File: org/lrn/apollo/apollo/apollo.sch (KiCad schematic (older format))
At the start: 68 parts, among them J10 Conn_01x01_Male, J11 Conn_01x01_Male, J12 Conn_01x01_Male, J13 Conn_01x01_Male, J17 Conn_01x01_Male, J18 Conn_01x01_Male, J4 Conn_01x01_Male, J6 Conn_01x01_Male, J7 Conn_01x01_Male, J8 Conn_01x01_Male, J9 Conn_01x01_Male, Q1 PN2222A, Q2 PN2222A, Q3 PN2222A, Q4 PN2222A, Q5 PN2222A, Q6 PN2222A, U1 74HC595, U2 5461AS-1, U3 74HC595, U4 ATmega168P-20PU

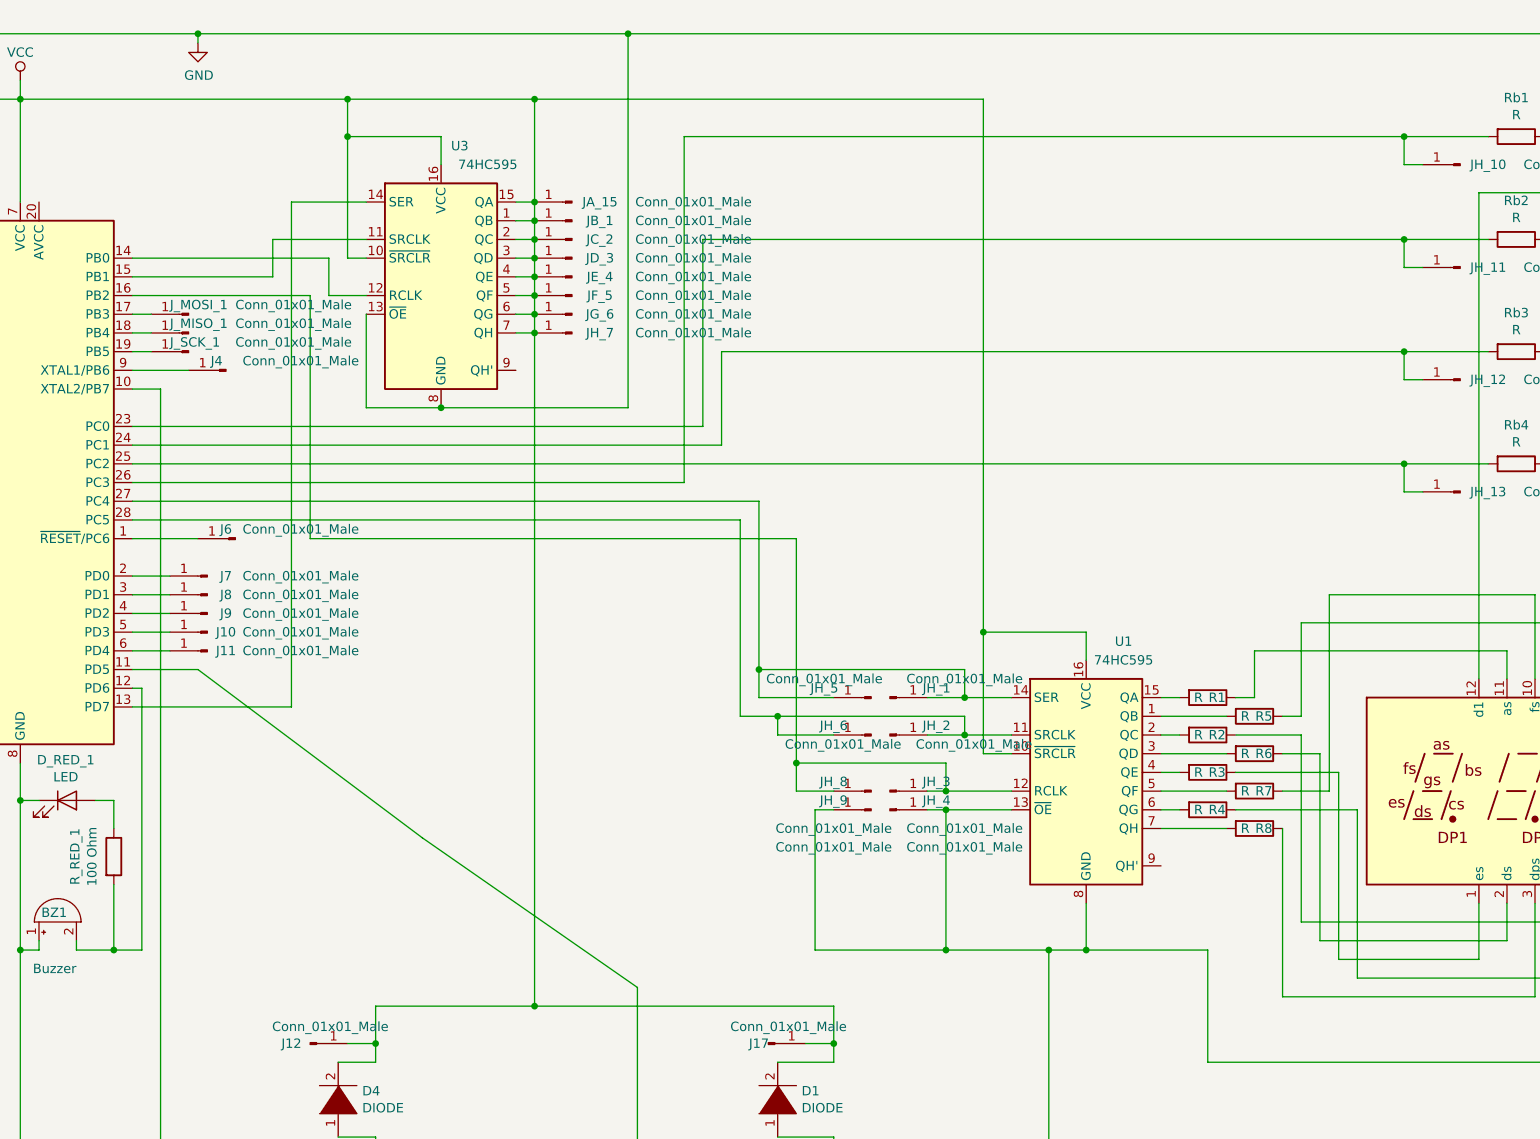
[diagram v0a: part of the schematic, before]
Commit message: apollo: remove wrong junctions
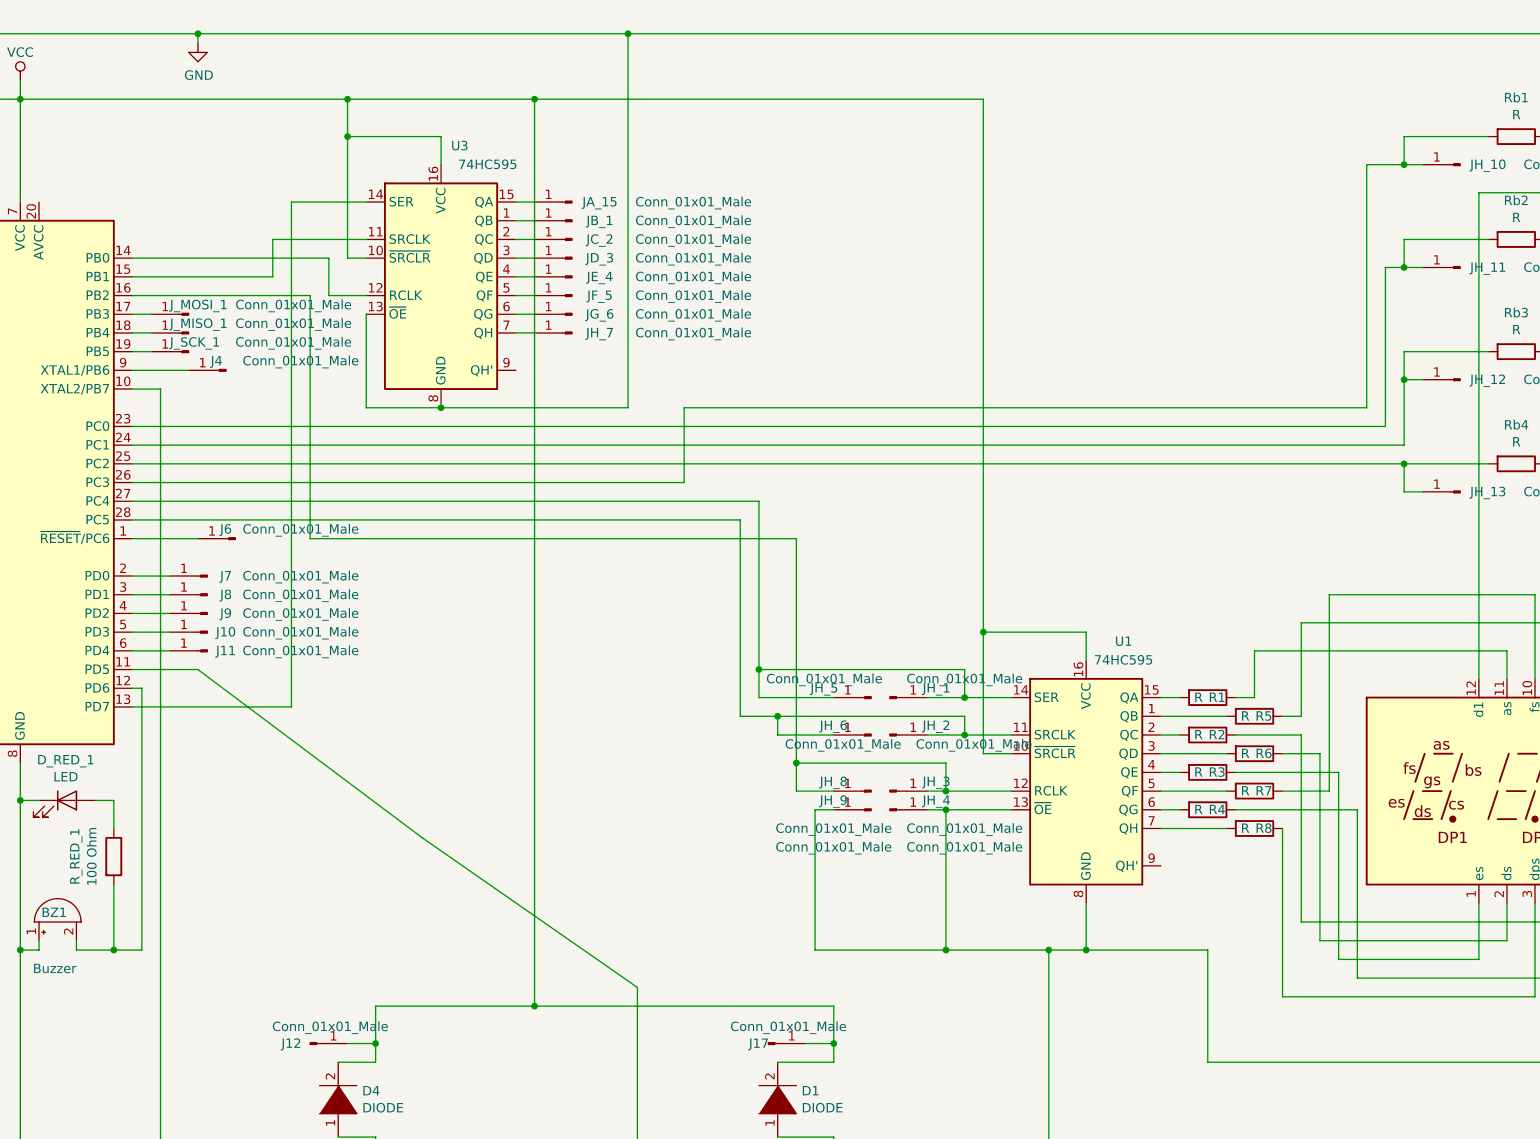
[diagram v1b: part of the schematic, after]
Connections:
- net VCC: no longer JA_15.1 (Pin_1), JB_1.1 (Pin_1), JC_2.1 (Pin_1), JD_3.1 (Pin_1), JE_4.1 (Pin_1), JF_5.1 (Pin_1), JG_6.1 (Pin_1), JH_7.1 (Pin_1), U3.1 (QB), U3.15 (QA), U3.2 (QC), U3.3 (QD), U3.4 (QE), U3.5 (QF), U3.6 (QG), U3.7 (QH)
- new net: JB_1.1 (Pin_1), U3.1 (QB)
- new net: JA_15.1 (Pin_1), U3.15 (QA)
- new net: JC_2.1 (Pin_1), U3.2 (QC)
- new net: JD_3.1 (Pin_1), U3.3 (QD)
- new net: JE_4.1 (Pin_1), U3.4 (QE)
- new net: JF_5.1 (Pin_1), U3.5 (QF)
- new net: JG_6.1 (Pin_1), U3.6 (QG)
- new net: JH_7.1 (Pin_1), U3.7 (QH)
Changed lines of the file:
@@
 	3600 2600 3200 2600
-Wire Wire Line
-	5000 2700 5000 1700
-Wire Wire Line
-	1950 2700 5000 2700
-Wire Wire Line
-	1950 2800 5100 2800
-Wire Wire Line
-	5100 2800 5100 2300
-Wire Wire Line
-	4900 1150 4900 3000
 Wire Wire Line
 	6500 950  6500 3800
@@
 	1950 2900 8750 2900
 Wire Wire Line
-	5000 1700 8750 1700
-Wire Wire Line
-	5100 2300 8750 2300
-Wire Wire Line
 	8850 1850 8750 1850
 Wire Wire Line
 	8750 1850 8750 1700
-Connection ~ 8750 1700
 Wire Wire Line
 	8750 1700 9200 1700
@@
 Wire Wire Line
 	8750 2450 8750 2300
-Connection ~ 8750 2300
 Wire Wire Line
 	8750 2300 9200 2300
@@
 	9500 1150 10000 1150
 Wire Wire Line
-	4900 1150 8750 1150
-Wire Wire Line
 	10300 950  10300 850
 Wire Wire Line
@@
 Wire Wire Line
 	8750 1300 8750 1150
-Connection ~ 8750 1150
 Wire Wire Line
 	8750 1150 9200 1150
@@
 Wire Wire Line
 	5700 7700 6850 7700
-Wire Wire Line
-	4100 950  4100 1500
 Connection ~ 4100 950
 Wire Wire Line
@@
 Wire Wire Line
 	4100 5800 5700 5800
-Connection ~ 4100 1500
-Wire Wire Line
-	4100 1500 4100 1600
-Connection ~ 4100 1600
-Wire Wire Line
-	4100 1600 4100 1700
-Connection ~ 4100 1700
-Wire Wire Line
-	4100 1700 4100 1800
-Connection ~ 4100 1800
-Wire Wire Line
-	4100 1800 4100 1900
-Connection ~ 4100 1900
-Wire Wire Line
-	4100 1900 4100 2000
-Connection ~ 4100 2000
-Wire Wire Line
-	4100 2000 4100 2100
-Connection ~ 4100 2100
-Wire Wire Line
-	4100 2100 4100 2200
-Connection ~ 4100 2200
-Wire Wire Line
-	4100 2200 4100 5800
 $Comp
 L Connector:USB_B_Micro J_USB_1
@@
 Wire Wire Line
 	1350 850  1350 950
+Wire Wire Line
+	4100 950  4100 5800
+Wire Wire Line
+	8750 2800 8750 2450
+Connection ~ 8750 2450
+Wire Wire Line
+	1950 2800 8750 2800
+Wire Wire Line
+	8650 2700 8650 1850
+Wire Wire Line
+	8650 1850 8750 1850
+Connection ~ 8750 1850
+Wire Wire Line
+	1950 2700 8650 2700
+Wire Wire Line
+	4900 2600 8550 2600
+Wire Wire Line
+	8550 2600 8550 1300
+Wire Wire Line
+	8550 1300 8750 1300
+Wire Wire Line
+	4900 2600 4900 3000
+Connection ~ 8750 1300
 $EndSCHEMATC

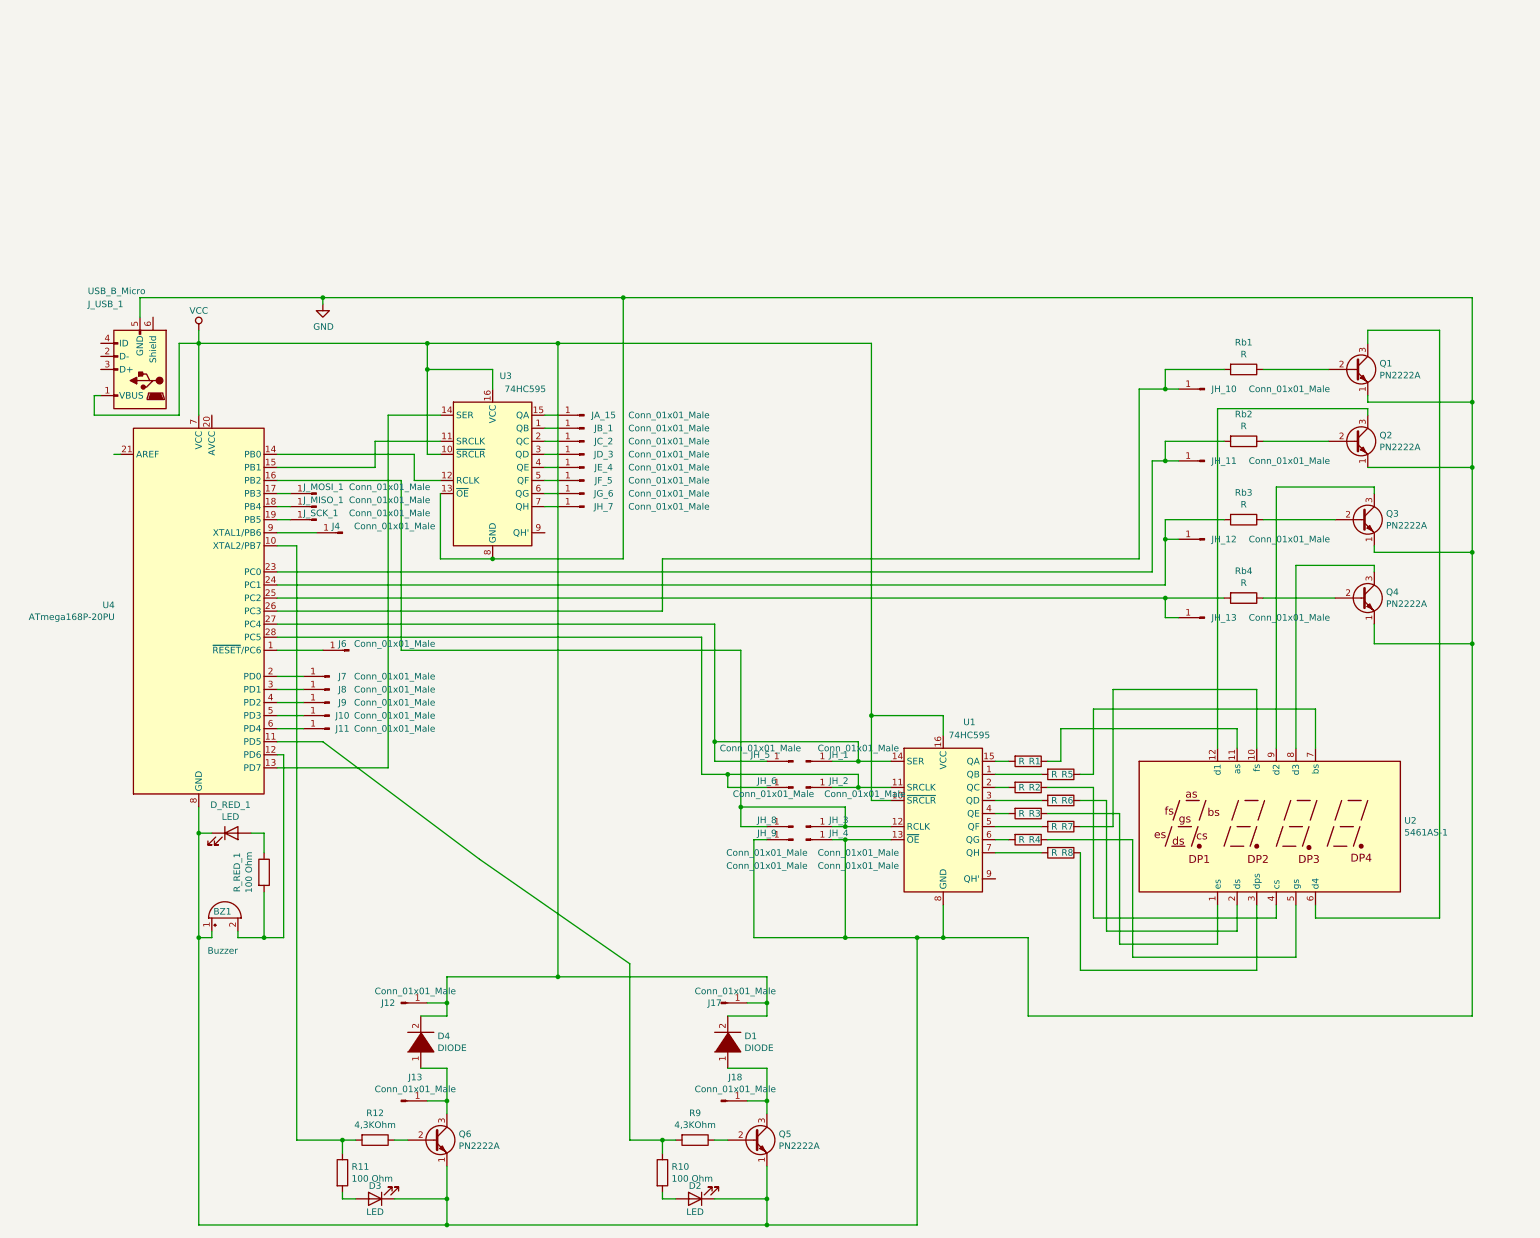
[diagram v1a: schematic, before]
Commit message: apollo: keybard added
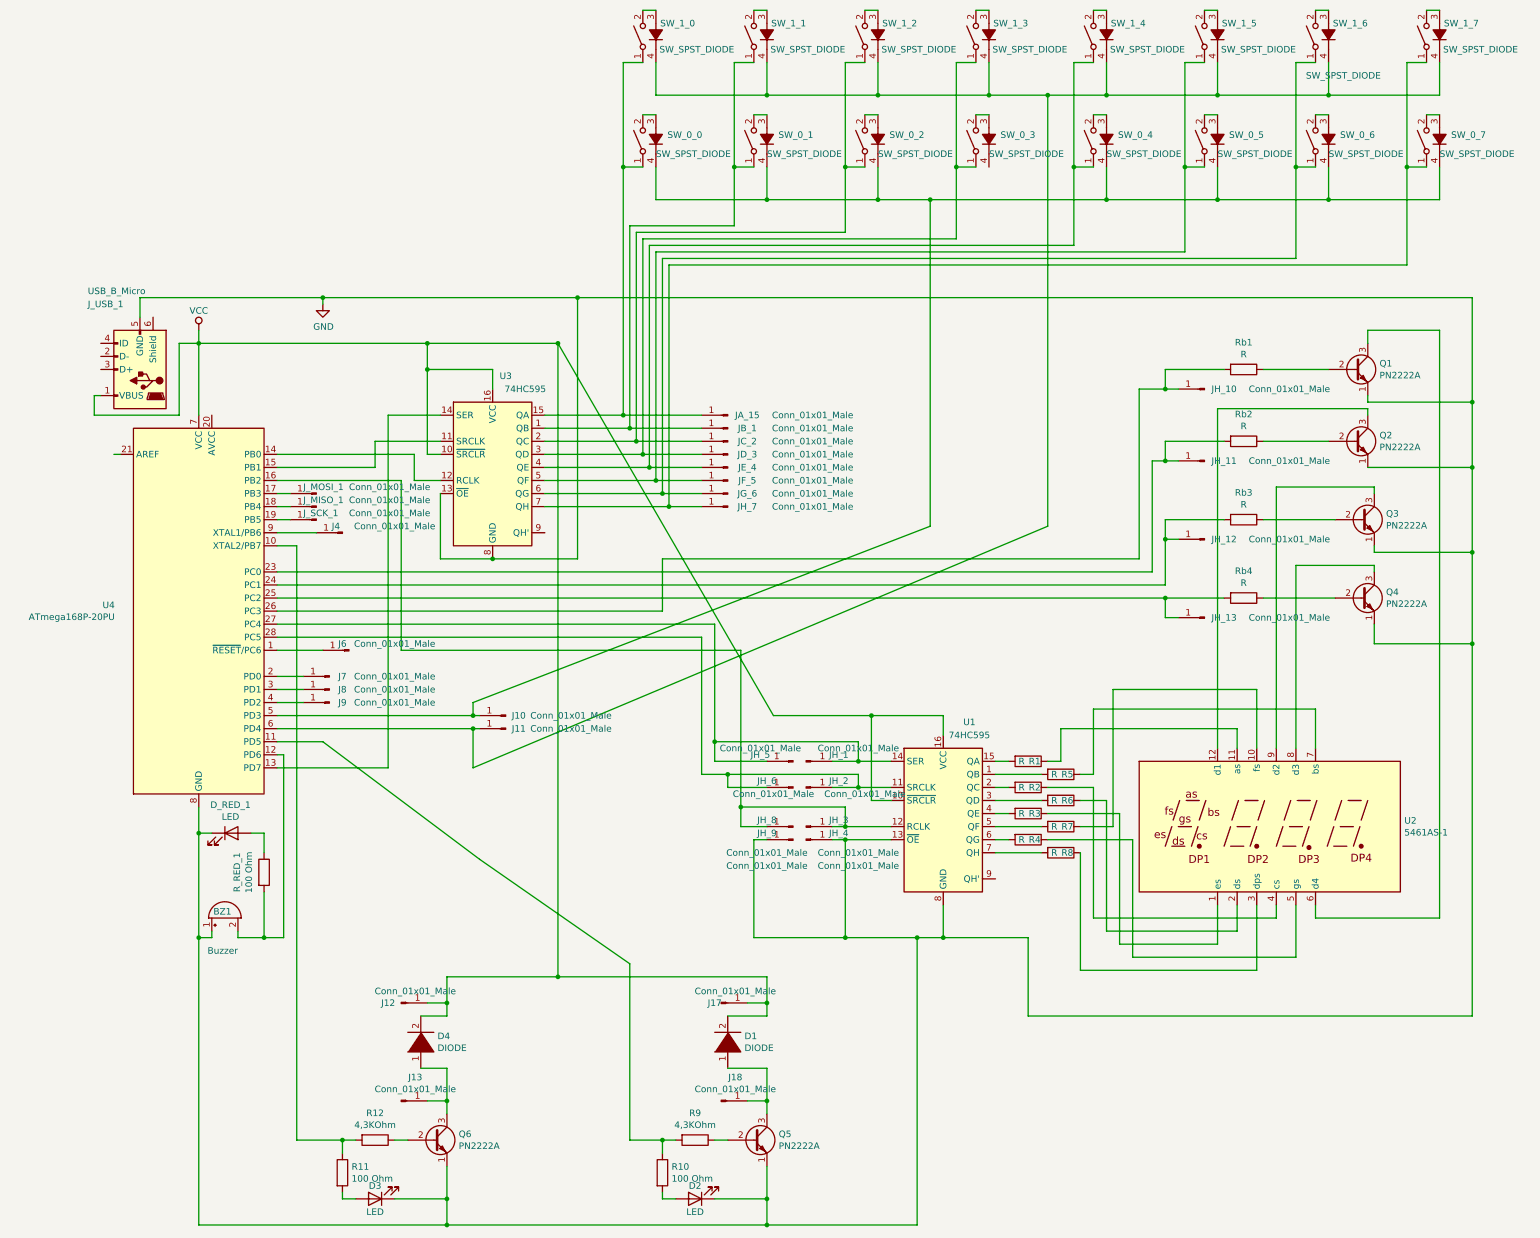
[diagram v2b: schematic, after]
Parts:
- added SW_0_0, SW_0_1, SW_0_2, SW_0_3, SW_0_4, SW_0_5, SW_0_6, SW_0_7, SW_1_0, SW_1_1, SW_1_2, SW_1_3, SW_1_4, SW_1_5, SW_1_6, SW_1_7: SW_SPST_DIODE, apollo:gateron, symbol apollo:SW_SPST_DIODE
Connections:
- net at JB_1.1 (Pin_1), U3.1 (QB): now also SW_0_1.1, SW_1_1.1
- net at JA_15.1 (Pin_1), U3.15 (QA): now also SW_0_0.1, SW_1_0.1
- net at JC_2.1 (Pin_1), U3.2 (QC): now also SW_0_2.1, SW_1_2.1
- net at JD_3.1 (Pin_1), U3.3 (QD): now also SW_0_3.1, SW_1_3.1
- net at JE_4.1 (Pin_1), U3.4 (QE): now also SW_0_4.1, SW_1_4.1
- net at JF_5.1 (Pin_1), U3.5 (QF): now also SW_0_5.1, SW_1_5.1
- net at JG_6.1 (Pin_1), U3.6 (QG): now also SW_0_6.1, SW_1_6.1
- net at JH_7.1 (Pin_1), U3.7 (QH): now also SW_0_7.1, SW_1_7.1
- net at J10.1 (Pin_1), U4.5 (PD3): now also SW_0_0.4 (A), SW_0_1.4 (A), SW_0_2.4 (A), SW_0_4.4 (A), SW_0_5.4 (A), SW_0_6.4 (A), SW_0_7.4 (A)
- net at J11.1 (Pin_1), U4.6 (PD4): now also SW_1_0.4 (A), SW_1_1.4 (A), SW_1_2.4 (A), SW_1_3.4 (A), SW_1_4.4 (A), SW_1_5.4 (A), SW_1_6.4 (A), SW_1_7.4 (A)
- new net: SW_1_0.2, SW_1_0.3 (K)
- new net: SW_0_0.2, SW_0_0.3 (K)
- new net: SW_1_1.2, SW_1_1.3 (K)
- new net: SW_0_1.2, SW_0_1.3 (K)
- new net: SW_1_2.2, SW_1_2.3 (K)
- new net: SW_0_2.2, SW_0_2.3 (K)
- new net: SW_1_3.2, SW_1_3.3 (K)
- new net: SW_0_3.2, SW_0_3.3 (K)
- new net: SW_1_4.2, SW_1_4.3 (K)
- new net: SW_0_4.2, SW_0_4.3 (K)
- new net: SW_1_5.2, SW_1_5.3 (K)
- new net: SW_0_5.2, SW_0_5.3 (K)
- new net: SW_1_6.2, SW_1_6.3 (K)
- new net: SW_0_6.2, SW_0_6.3 (K)
- new net: SW_1_7.2, SW_1_7.3 (K)
- new net: SW_0_7.2, SW_0_7.3 (K)
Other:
- moved on the sheet: J10, J11, JA_15, JB_1, JC_2, JD_3, JE_4, JF_5, JG_6, JH_7

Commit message: apollo: keubord linked in pcb
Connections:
- net at J10.1 (Pin_1), SW_0_0.4 (A), SW_0_1.4 (A)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: now also SW_0_3.4 (A)
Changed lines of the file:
@@
 	4850 -150 5700 -150
 Wire Wire Line
-	6950 -150 8300 -150
+	6950 -150 7400 -150
 Wire Wire Line
 	10850 -150 10850 -400
@@
 Wire Wire Line
 	3450 3900 3500 3900
+Wire Wire Line
+	7400 -400 7400 -150
+Connection ~ 7400 -150
+Wire Wire Line
+	7400 -150 8300 -150
 $EndSCHEMATC

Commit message: replace R100-Ohm resistors for 7-segment to smd
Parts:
- R1, R2, R3, R4, R5, R6, R7, R8: footprint apollo:R__Horizontal -> Resistor_SMD:R_1206_3216Metric_Pad1.42x1.75mm_HandSolder
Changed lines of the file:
@@
 F 0 "R7" V 7950 4700 50  0000 C CNN
 F 1 "R" V 7950 4600 50  0000 C CNN
-F 2 "apollo:R__Horizontal" V 7880 4650 50  0001 C CNN
+F 2 "Resistor_SMD:R_1206_3216Metric_Pad1.42x1.75mm_HandSolder" V 7880 4650 50  0001 C CNN
 F 3 "~" H 7950 4650 50  0001 C CNN
 	1    7950 4650
@@
 F 0 "R5" V 7950 4300 50  0000 C CNN
 F 1 "R" V 7950 4200 50  0000 C CNN
-F 2 "apollo:R__Horizontal" V 7880 4250 50  0001 C CNN
+F 2 "Resistor_SMD:R_1206_3216Metric_Pad1.42x1.75mm_HandSolder" V 7880 4250 50  0001 C CNN
 F 3 "~" H 7950 4250 50  0001 C CNN
 	1    7950 4250
@@
 F 0 "R2" V 7700 4400 50  0000 C CNN
 F 1 "R" V 7700 4300 50  0000 C CNN
-F 2 "apollo:R__Horizontal" V 7630 4350 50  0001 C CNN
+F 2 "Resistor_SMD:R_1206_3216Metric_Pad1.42x1.75mm_HandSolder" V 7630 4350 50  0001 C CNN
 F 3 "~" H 7700 4350 50  0001 C CNN
 	1    7700 4350
@@
 F 0 "R1" V 7700 4200 50  0000 C CNN
 F 1 "R" V 7700 4100 50  0000 C CNN
-F 2 "apollo:R__Horizontal" V 7630 4150 50  0001 C CNN
+F 2 "Resistor_SMD:R_1206_3216Metric_Pad1.42x1.75mm_HandSolder" V 7630 4150 50  0001 C CNN
 F 3 "~" H 7700 4150 50  0001 C CNN
 	1    7700 4150
@@
 F 0 "R6" V 7950 4500 50  0000 C CNN
 F 1 "R" V 7950 4400 50  0000 C CNN
-F 2 "apollo:R__Horizontal" V 7880 4450 50  0001 C CNN
+F 2 "Resistor_SMD:R_1206_3216Metric_Pad1.42x1.75mm_HandSolder" V 7880 4450 50  0001 C CNN
 F 3 "~" H 7950 4450 50  0001 C CNN
 	1    7950 4450
@@
 F 0 "R3" V 7700 4600 50  0000 C CNN
 F 1 "R" V 7700 4500 50  0000 C CNN
-F 2 "apollo:R__Horizontal" V 7630 4550 50  0001 C CNN
+F 2 "Resistor_SMD:R_1206_3216Metric_Pad1.42x1.75mm_HandSolder" V 7630 4550 50  0001 C CNN
 F 3 "~" H 7700 4550 50  0001 C CNN
 	1    7700 4550
@@
 F 0 "R4" V 7700 4800 50  0000 C CNN
 F 1 "R" V 7700 4700 50  0000 C CNN
-F 2 "apollo:R__Horizontal" V 7630 4750 50  0001 C CNN
+F 2 "Resistor_SMD:R_1206_3216Metric_Pad1.42x1.75mm_HandSolder" V 7630 4750 50  0001 C CNN
 F 3 "~" H 7700 4750 50  0001 C CNN
 	1    7700 4750
@@
 F 0 "R8" V 7950 4900 50  0000 C CNN
 F 1 "R" V 7950 4800 50  0000 C CNN
-F 2 "apollo:R__Horizontal" V 7880 4850 50  0001 C CNN
+F 2 "Resistor_SMD:R_1206_3216Metric_Pad1.42x1.75mm_HandSolder" V 7880 4850 50  0001 C CNN
 F 3 "~" H 7950 4850 50  0001 C CNN
 	1    7950 4850

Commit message: apollo: pcb regularization
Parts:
- D1, D4: footprint apollo:D__Horizontal -> Diode_SMD:D_0805_2012Metric_Pad1.15x1.40mm_HandSolder
- J10, J11, J12, J13, J17, J18, J4, J6, J7, J8, J9, JA_15, JB_1, JC_2, JD_3, JE_4, JF_5, JG_6, JH_1, JH_10, JH_11, JH_12, JH_13, JH_2, JH_3, JH_4, JH_5, JH_6, JH_7, JH_8, JH_9, J_MISO_1, J_MOSI_1, J_SCK_1: footprint Connector_Pin:Pin_D0.7mm_L6.5mm_W1.8mm_FlatFork -> Connector_Pin:Pin_D1.0mm_L10.0mm
- Q1, Q2, Q3, Q4, Q5, Q6: footprint apollo:2N222A-TO-92_Wide -> Package_TO_SOT_SMD:SOT-23
- R10, R11, R12, R9, R_RED_1, Rb1, Rb2, Rb3, Rb4: footprint apollo:R__Horizontal -> Resistor_SMD:R_1206_3216Metric_Pad1.42x1.75mm_HandSolder
